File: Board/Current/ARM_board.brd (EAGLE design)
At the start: 101.6 x 81.3 mm, 175 parts, among them IC3 STM32F437VI, IC4 LM358DT, J1 USART/I2C, J10 ANALOG, J11 DGND, J12 DPWR, J13 DIGITAL, J14 SGND, J15 SPWR, J16 SERVO, J2 I2C2/USART3, J3 USART2, J5 SPI, J6 Bluesmirf, J7 SWD, J8 AGND, J9 APWR, Q1 STL4P2UH7, Q2 2STR1230, Q3 STL4P2UH7, SW1 SW, U1 LSM330, U10 BAV99, U11 BAV99, U12 USBLC6-2, U13 USBLC6-2, U14 STMPS2171MTR, U15 MC74HC164, U3 NC7SZU04, U4 L6206Q, U5 L6206Q, U6 SI7617, U7 SI7617, U8 SI7617, U9 SI7617, Y2 8MHz

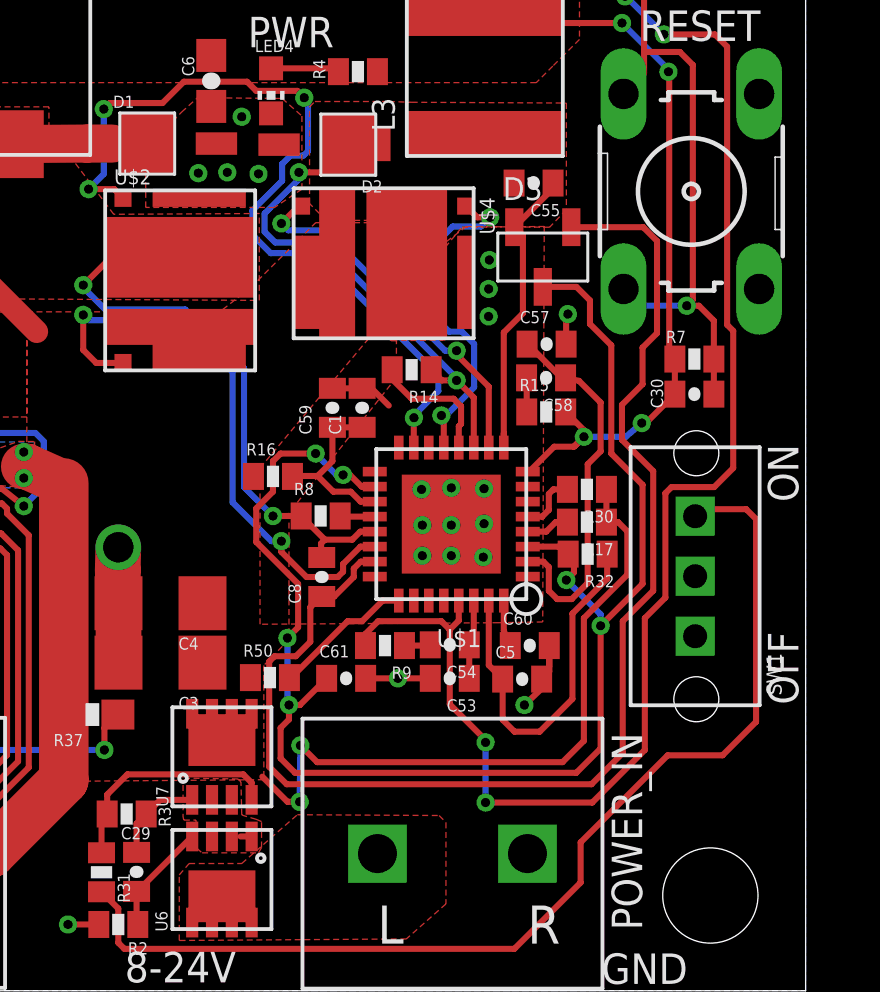
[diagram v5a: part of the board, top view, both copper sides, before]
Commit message: Addressed switching regulator comments.
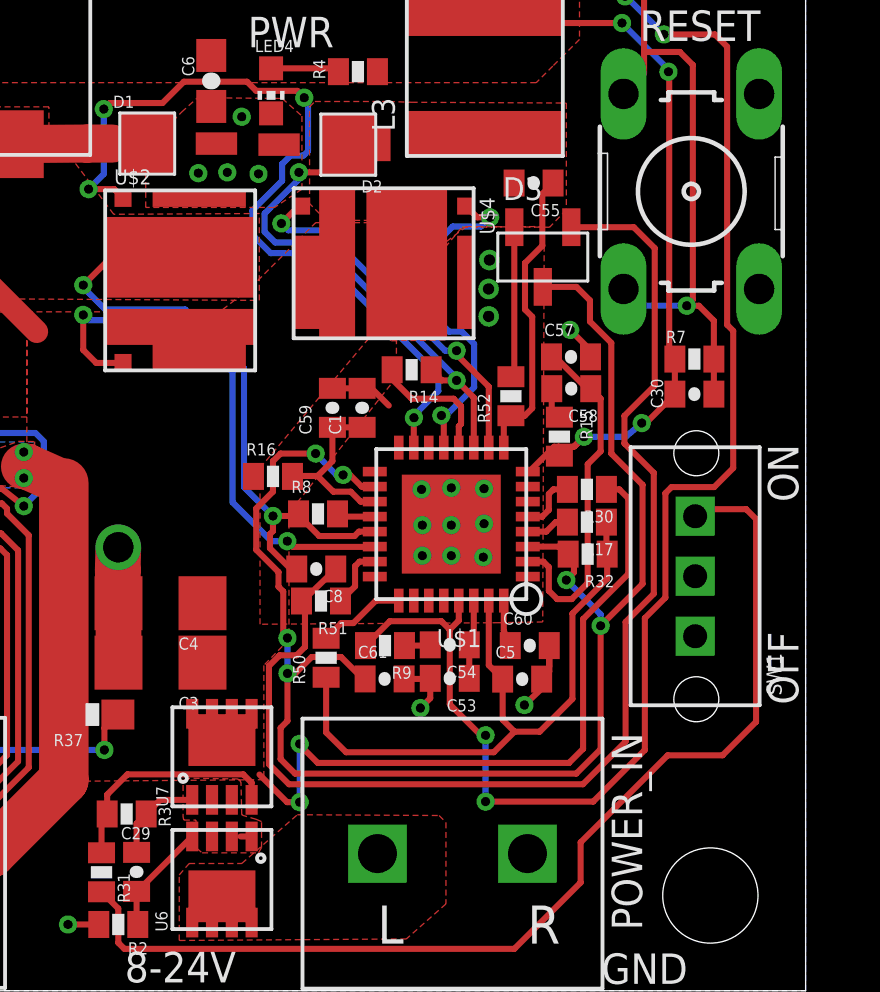
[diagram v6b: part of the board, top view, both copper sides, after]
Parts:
- added R51, R52: 10, SparkFun:0402-RES
- moved R50 1.99 mm to (85.6, 11.1), turned to 90 degrees
- moved C61 1.28 mm to (87.6, 10.4)
- moved R15 0.93 mm to (93.4, 18.5), turned to 270 degrees
- moved C57 0.92 mm to (93.8, 21.1)
- moved C58 0.91 mm to (93.8, 20.1)
- moved C8 0.32 mm to (85.3, 14.1), turned to 180 degrees
- moved R8 0.11 mm to (85.3, 15.9)
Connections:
- new net N$15: C5.1, R17.1, R32.1, R50.1, U$1.31
- new net N$59: C55.1, R52.1, U$1.9
- net BOOT3: now also R52.2; no longer C55.1, U$1.9
- net N$20: now also R51.1, U$1.23; no longer C5.1, R32.1, U$1.31
- net N$25: now also R51.2; no longer U$1.23
- net VIN: no longer R17.1, R50.1
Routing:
- net N$15: track 0.00 -> 22.2 mm
- net N$20: track 12.4 -> 2.11 mm
- net N$59: track 0.00 -> 9.97 mm
- net BOOT3: track 10.2 -> 5.03 mm
- net N$84: track 4.87 -> 2.94 mm
- net N$25: track 43.1 -> 41.4 mm
- net N$66: track 25.2 -> 26.9 mm
- net LDO5: track 50.4 -> 51.6 mm
- net N$56: track 19.3 -> 18.1 mm
- net N$77: track 12.7 -> 11.7 mm
- net +3V3: track 379.6 -> 378.9 mm

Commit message: Cleaned up the layout.
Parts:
- moved R20 2.42 mm to (56.6, 33.9), turned to 180 degrees
- moved R38 1.03 mm to (53.0, 7.11)
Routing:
- net M0_B: track 79.2 -> 87.3 mm
- net +3V3: track 378.9 -> 372.1 mm
- net USART2_RX: track 39.6 -> 46.3 mm, vias 7 -> 6
- net BOOT1: track 108.6 -> 104.5 mm
- net M0_FAULT: track 93.3 -> 97.3 mm
- net SPI3_MISO: track 128.0 -> 130.4 mm
- net BTN1: track 118.4 -> 116.1 mm, vias 7 -> 5
- net SPI3_MOSI: track 128.4 -> 130.5 mm
- net SPI3_SCK: track 129.6 -> 131.7 mm
- net SPI3_NSS: track 122.4 -> 124.5 mm
- net SPI1_NSS: track 38.7 -> 36.7 mm, vias 6 -> 5
- net BAT_SENSE: track 36.2 -> 34.3 mm, vias 6 -> 4
- net GND: track 152.5 -> 150.6 mm
- net I2C2_SCL/USART3_TX: track 74.5 -> 76.2 mm
- net M1_EN: track 116.8 -> 118.3 mm
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
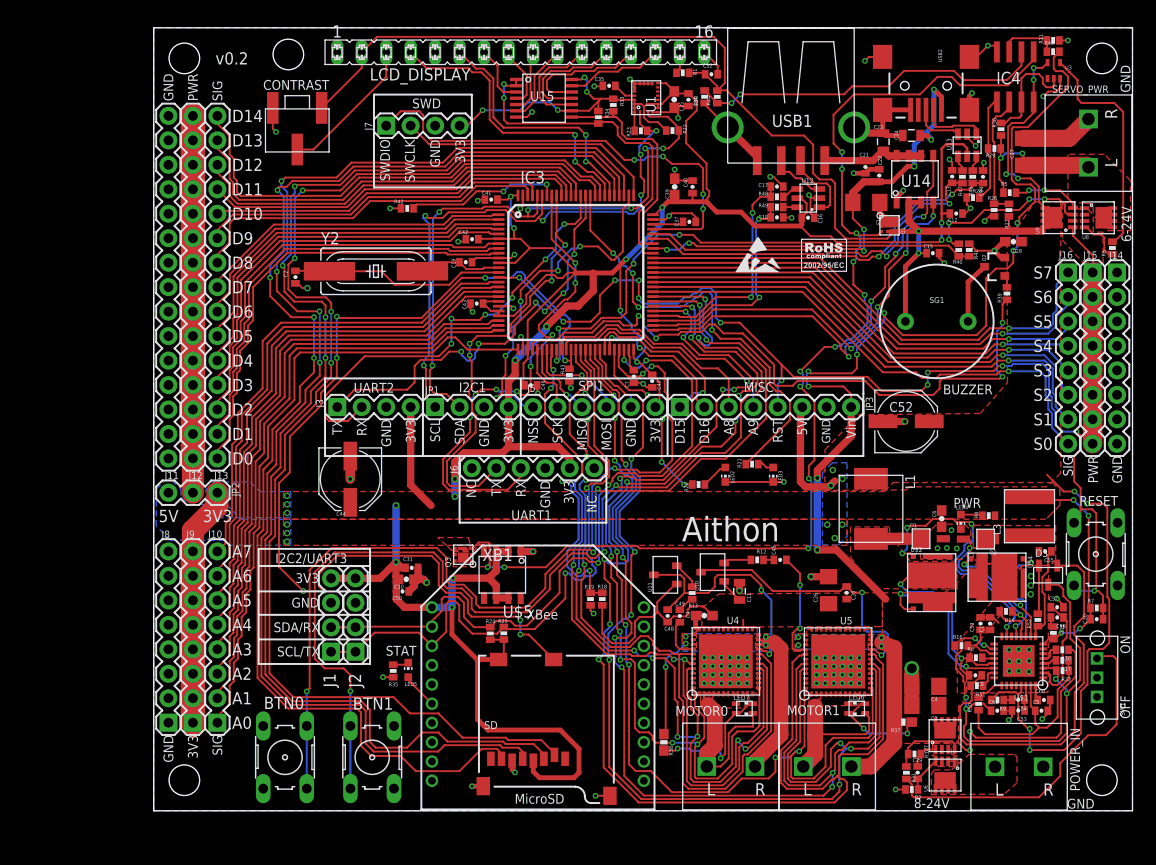
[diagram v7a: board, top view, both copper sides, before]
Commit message: Fixed the size of the 680uF capacitors. Added new voltage divider on SHDWN pin of switching controller.
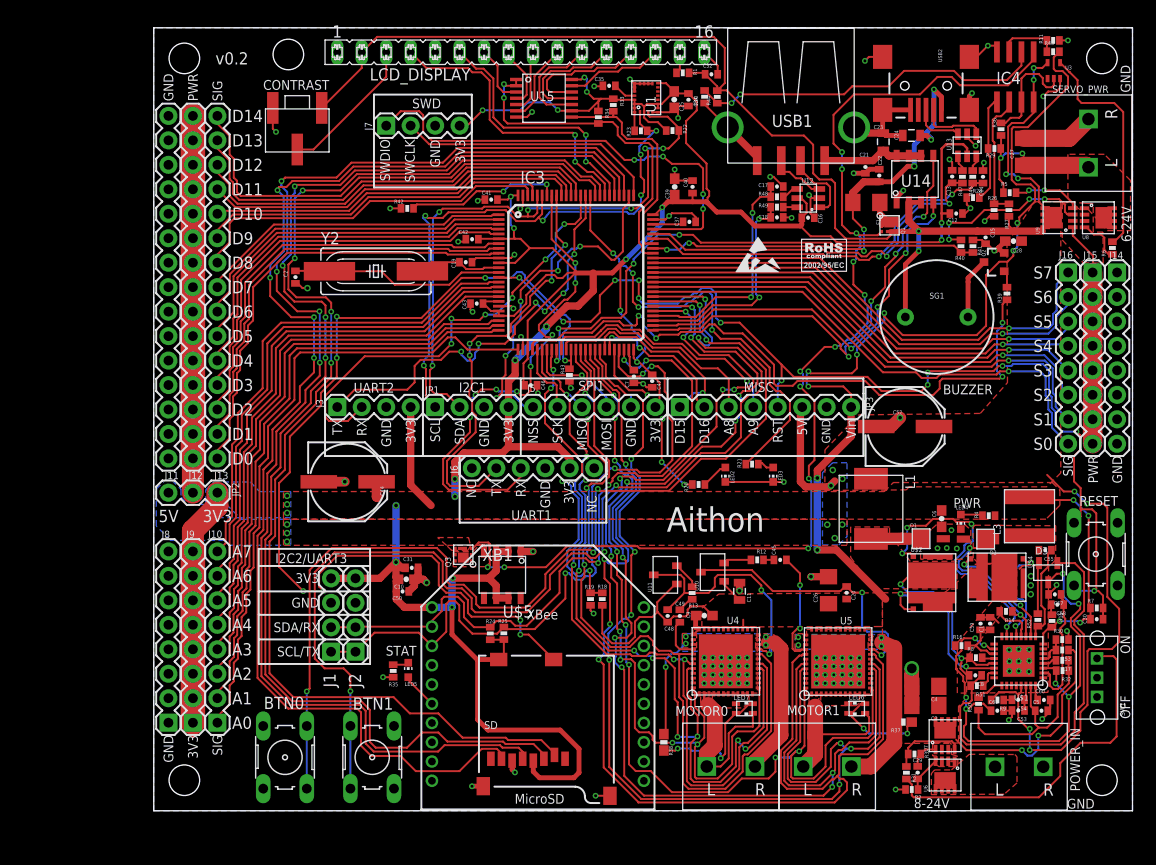
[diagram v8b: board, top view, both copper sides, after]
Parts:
- added R53: 330k, SparkFun:0402-RES
- C44, C52: device SparkFun:PANASONIC_D -> SparkFun:PANASONIC_E
- moved C15 5.71 mm to (86.3, 59.5), turned to 270 degrees
- moved C57 1.36 mm to (93.5, 22.5), turned to 180 degrees
- moved C58 1.33 mm to (93.8, 21.4)
- moved R15 1.25 mm to (93.2, 19.7)
- moved R30 1.06 mm to (94.3, 17.8), turned to 0 degrees
- moved R41 0.54 mm to (85.0, 58.6)
- moved C52 0.53 mm to (78.0, 39.9)
- moved Q2 0.49 mm to (87.3, 57.0)
- moved SG1 0.46 mm to (81.3, 51.3)
- moved R40 0.46 mm to (83.8, 58.6)
- moved C44 0.38 mm to (20.1, 34.2), turned to 0 degrees
- moved D3 0.26 mm to (92.8, 24.7)
- moved C55 0.13 mm to (92.5, 27.1)
- moved C28 0.06 mm to (89.2, 59.1)
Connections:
- net GND: now also R30.2
- net N$82: now also R30.1, R53.2; no longer R30.2
- net VIN: now also R53.1; no longer R30.1
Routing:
- net LDO5: track 51.6 -> 54.8 mm, vias 6 -> 8
- net N$77: track 11.7 -> 13.3 mm
- net +3V3: track 372.1 -> 373.3 mm
- net N$82: track 2.01 -> 3.08 mm
- net VIN: track 145.1 -> 144.2 mm
- net 5V: track 204.1 -> 204.9 mm
- net N$10: track 36.2 -> 37.0 mm
- net N$65: track 1.27 -> 1.78 mm
